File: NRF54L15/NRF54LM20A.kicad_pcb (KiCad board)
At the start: 4 copper layers, 40.1 x 22 mm, 75 parts, among them IC2 BQ51013B, IC3 NMH1000T1, IC4 ST1PS02B1QTR, J1 Conn_ARM_SWD_TagConnect_TC203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, U1 S25HS512TFANHI010, U3 SR4W035, U4 IM67D128BV01, U5 TXS0102DQE, U6 LSM6DSV16B, U7 nRF54L15-QFXX, Y1 CX2016DB32000D0WZRC1

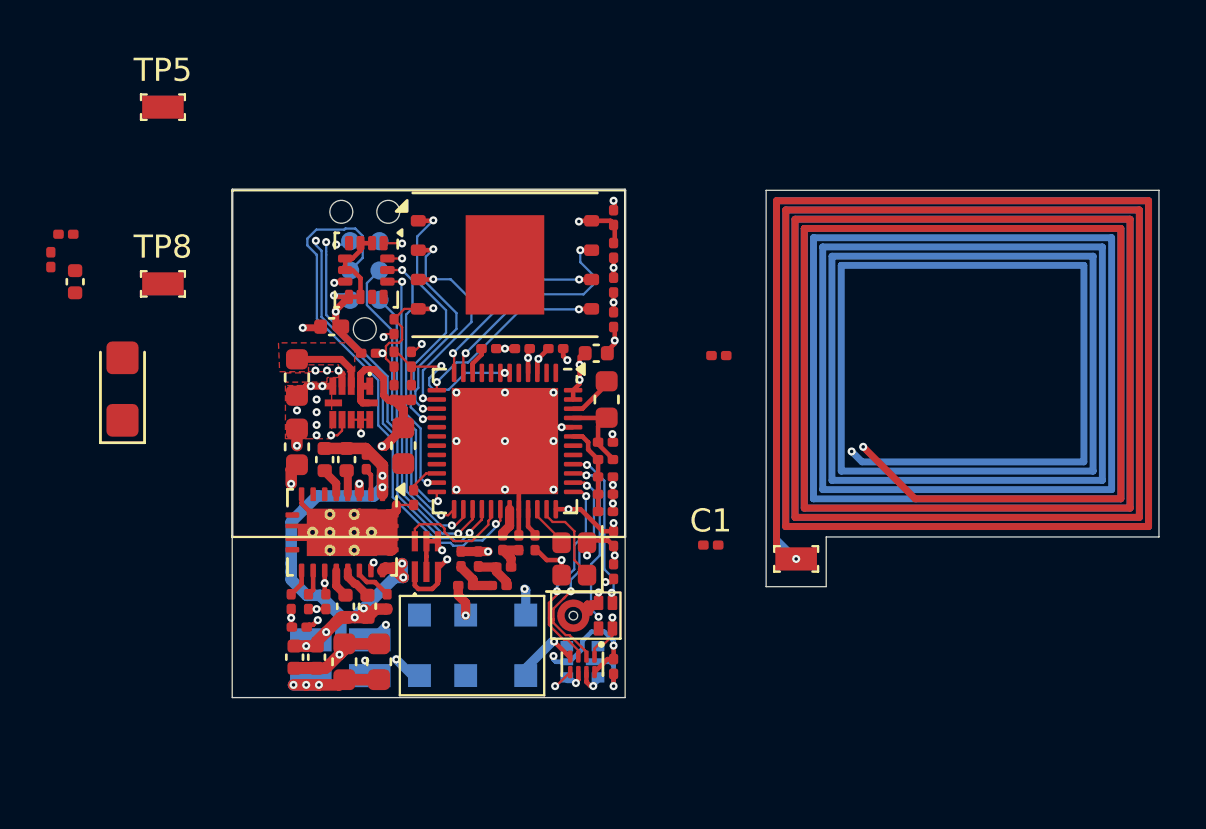
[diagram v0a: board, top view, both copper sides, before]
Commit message: nfc rect
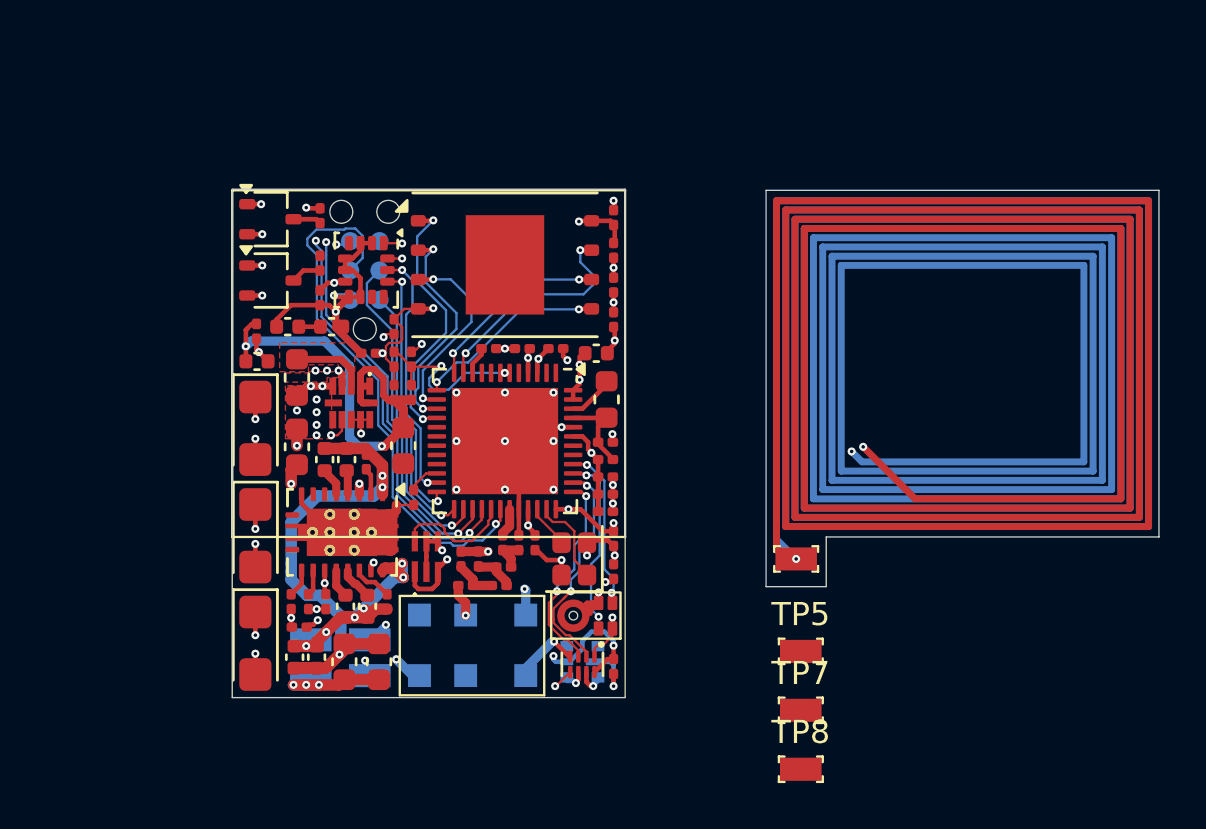
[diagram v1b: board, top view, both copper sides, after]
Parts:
- removed C1, C12: 0.1u, Capacitor_SMD:C_0201_0603Metric
- removed C42, C43: TBD, Capacitor_SMD:C_0201_0603Metric
- added C44: T527I107M006ATE070, Capacitor_Tantalum_SMD:CP_EIA-3216-12_Kemet-S, F.Cu at (87.8, 86.0)
- added C45: T527I107M006ATE070, Capacitor_Tantalum_SMD:CP_EIA-3216-12_Kemet-S, F.Cu at (87.8, 81.3)
- added C46: TBD, Capacitor_SMD:C_0201_0603Metric, F.Cu at (90.6, 74.2)
- added C47: TBD, Capacitor_SMD:C_0201_0603Metric, F.Cu at (90.6, 72.2)
- added C48: 0.1u, Capacitor_SMD:C_0201_0603Metric, F.Cu at (90.6, 75.7)
- added C49: 10u, Capacitor_SMD:C_0402_1005Metric, F.Cu at (87.9, 78.5)
- added C50: 0.1u, Capacitor_SMD:C_0201_0603Metric, F.Cu at (87.8, 77.2)
- added D2: BAT54SW, Package_TO_SOT_SMD:SOT-323_SC-70, F.Cu at (88.5, 75.0)
- added D3: BAT54SW, Package_TO_SOT_SMD:SOT-323_SC-70, F.Cu at (88.5, 72.3)
- added TP7: RCU-0C, digikey-footprints:PROBE_PAD_0603, F.Cu at (111.4, 93.5)
- moved TP5 36.3 mm to (111.4, 91.0)
- moved TP8 34.7 mm to (111.4, 96.1)
- moved C39 12.4 mm to (87.8, 90.7), turned to -90 degrees
- moved C25 9.40 mm to (89.2, 77.0), turned to 0 degrees
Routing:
- net +5V: track 29.1 -> 45.2 mm, vias 4 -> 10
- net NFC1: track 15.1 -> 22.4 mm
- net GND: track 59.6 -> 66.7 mm, vias 40 -> 46
- net DECA: track 5.11 -> 11.1 mm, vias 0 -> 2
- net NFC2: track 17.6 -> 23.3 mm
- net Net-(IC4-CL): track 1.54 -> 6.73 mm
- net +1V8: track 28.5 -> 31.7 mm
- net NFC_EH1: track 0.00 -> 1.33 mm
- net NFC_EH2: track 0.00 -> 1.22 mm
- added copper zone on In2.Cu, net +5V
